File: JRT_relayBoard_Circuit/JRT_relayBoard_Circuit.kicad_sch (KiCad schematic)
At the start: 0 parts

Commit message: 回路図を実装
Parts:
- added J1: Conn_ESP32_Left, symbol Connector:Conn_01x15_Socket
- added J2: Conn_ESP32_Right, symbol Connector:Conn_01x15_Socket
- added J3: 37212-62M3-003PL, CONN_37212-62M3-003PL_3MM, symbol 37212_62M3_003PL:37212-62M3-003PL
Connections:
- new net +3.3V: J1.1 (Pin_1)
- new net +9V: J2.1 (Pin_1)
- new net A1: J2.10 (Pin_10)
- new net A2: J2.11 (Pin_11)
- new net A3: J2.12 (Pin_12)
- new net A4: J2.13 (Pin_13)
- new net A5: J2.14 (Pin_14)
- new net D1: J1.3 (Pin_3)
- new net D10: J2.4 (Pin_4)
- new net D11: J2.5 (Pin_5)
- new net D12: J2.6 (Pin_6)
- new net D13: J2.7 (Pin_7)
- new net D14: J2.8 (Pin_8)
- new net D15: J2.9 (Pin_9)
- new net D2: J1.5 (Pin_5)
- new net D3: J1.8 (Pin_8), J1.9 (Pin_9)
- new net D5: J1.10 (Pin_10)
- new net D6: J1.11 (Pin_11)
- new net D7: J1.14 (Pin_14)
- new net D8: J1.15 (Pin_15)
- new net D9: J2.3 (Pin_3)
- new net GND: J2.2 (Pin_2)
- new net GND1: J1.2 (Pin_2)
- new net UART-RX: J1.6 (Pin_6)
- new net UART-TX: J1.7 (Pin_7)
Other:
- note added: "ESP32関係の配線 (ELEGOO ESP-32 開発ボード)"
- company: (none) -> (一社)次世代ロボットエンジニア支援機構
- title: (none) -> JRT中継基板Ver2.0

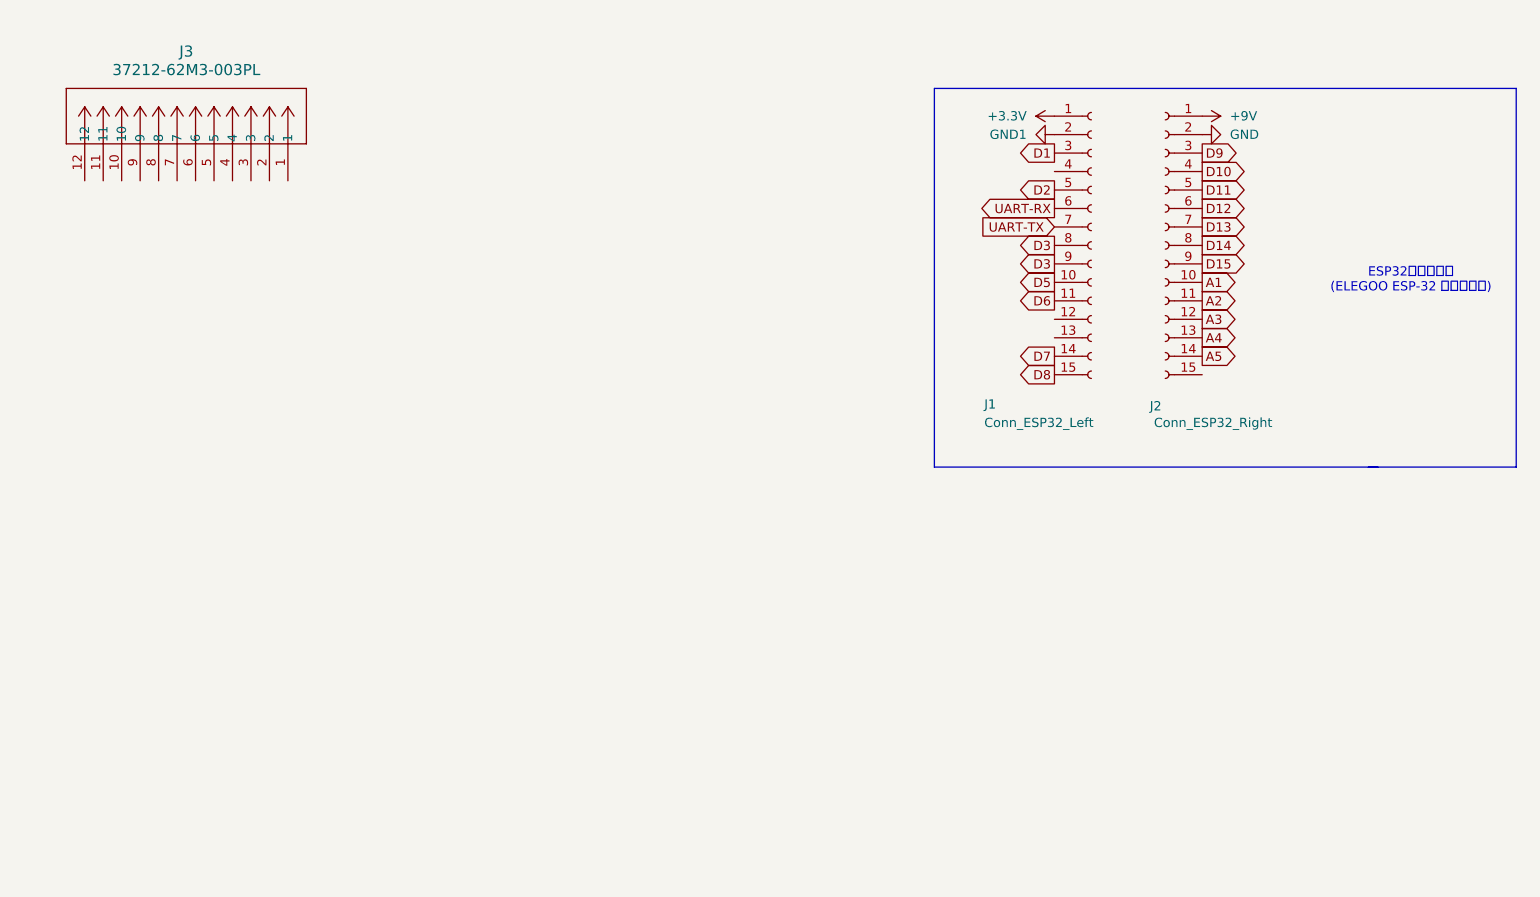
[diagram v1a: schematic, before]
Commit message: コネクタの配置をした
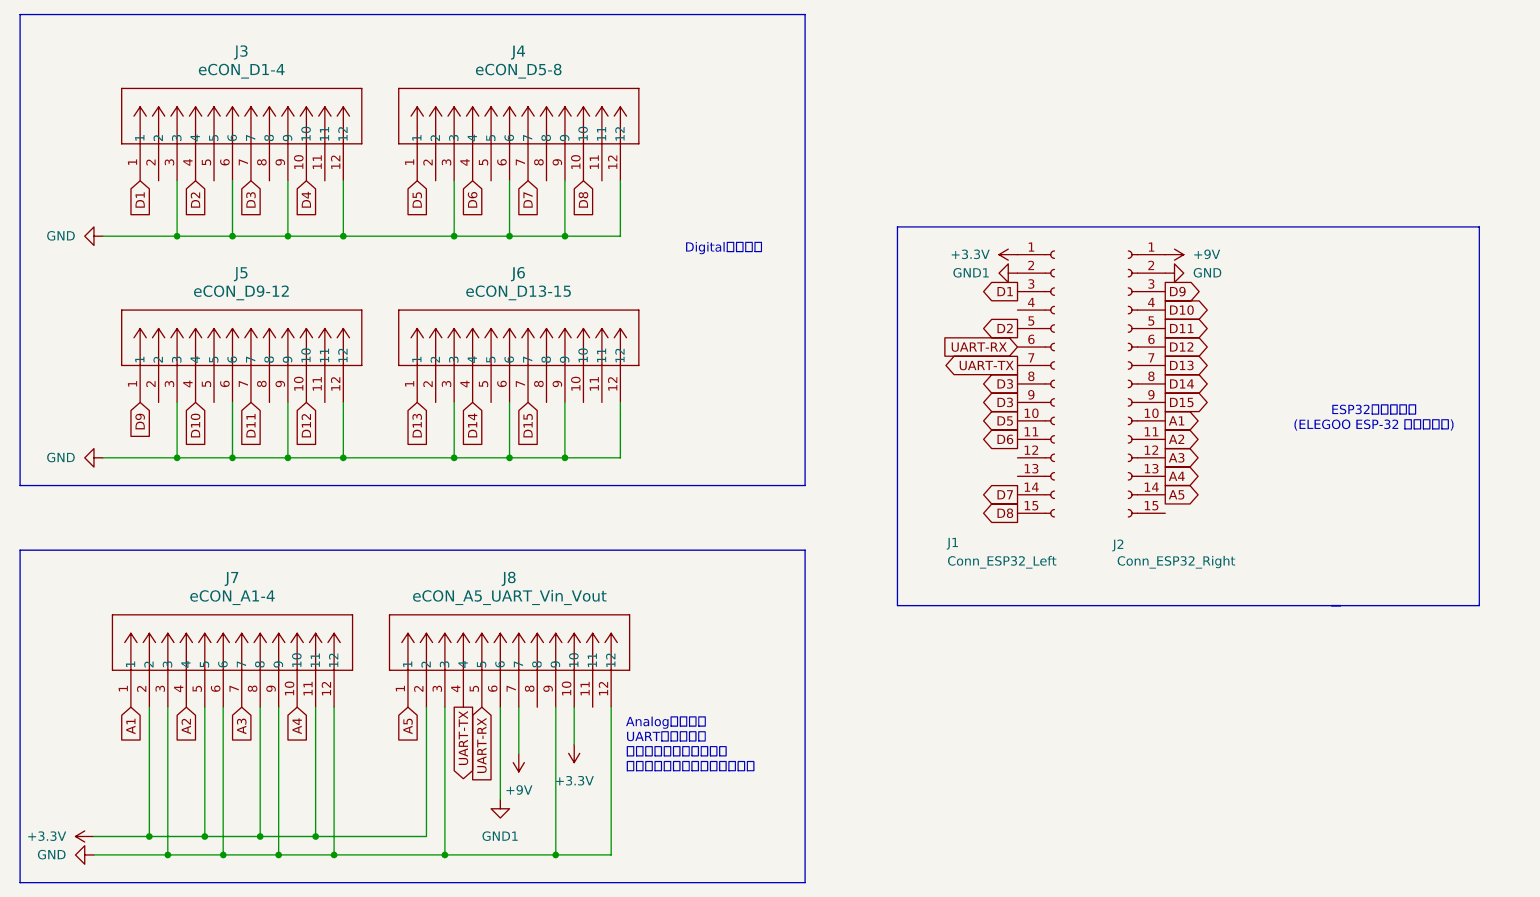
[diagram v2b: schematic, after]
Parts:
- added J4: eCON_D5-8, eCon:CONN_37212-62M3-003PL_3MM, symbol 37212_62M3_003PL:37212-62M3-003PL
- added J5: eCON_D9-12, eCon:CONN_37212-62M3-003PL_3MM, symbol 37212_62M3_003PL:37212-62M3-003PL
- added J6: eCON_D13-15, eCon:CONN_37212-62M3-003PL_3MM, symbol 37212_62M3_003PL:37212-62M3-003PL
- added J7: eCON_A1-4, eCon:CONN_37212-62M3-003PL_3MM, symbol 37212_62M3_003PL:37212-62M3-003PL
- added J8: eCON_A5_UART_Vin_Vout, eCon:CONN_37212-62M3-003PL_3MM, symbol 37212_62M3_003PL:37212-62M3-003PL
- J1, J2: footprint (none) -> Connector_PinSocket_2.54mm:PinSocket_1x15_P2.54mm_Vertical
- J3: value 37212-62M3-003PL -> eCON_D1-4; footprint CONN_37212-62M3-003PL_3MM -> eCon:CONN_37212-62M3-003PL_3MM
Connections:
- net +3.3V: now also J7.11, J7.2, J7.5, J7.8, J8.10, J8.2
- net +9V: now also J8.7
- net A1: now also J7.1
- net A2: now also J7.4
- net A3: now also J7.7
- net A4: now also J7.10
- net A5: now also J8.1
- net D1: now also J3.1
- net D10: now also J5.4
- net D11: now also J5.7
- net D12: now also J5.10
- net D13: now also J6.1
- net D14: now also J6.4
- net D15: now also J6.7
- net D2: now also J3.4
- net D3: now also J3.7
- net D5: now also J4.1
- net D6: now also J4.4
- net D7: now also J4.7
- net D8: now also J4.10
- net D9: now also J5.1
- net GND: now also J3.12, J3.3, J3.6, J3.9, J4.12, J4.3, J4.6, J4.9, J5.12, J5.3, J5.6, J5.9, J6.12, J6.3, J6.6, J6.9, J7.12, J7.3, J7.6, J7.9, J8.12, J8.3, J8.9
- net GND1: now also J8.6
- net UART-RX: now also J8.5
- net UART-TX: now also J8.4
- net D4: now reaches J3.10
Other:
- note added: "Analog入力端子 UART入出力端子 マイコン用電源入力端子 送信モジュール用電源出力端子"
- note added: "Digital入力端子"
- moved on the sheet: J1, J2, J3

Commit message: 配線を行った
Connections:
- net UART-RX: now also J8.4; no longer J8.5
- net UART-TX: now also J8.5; no longer J8.4

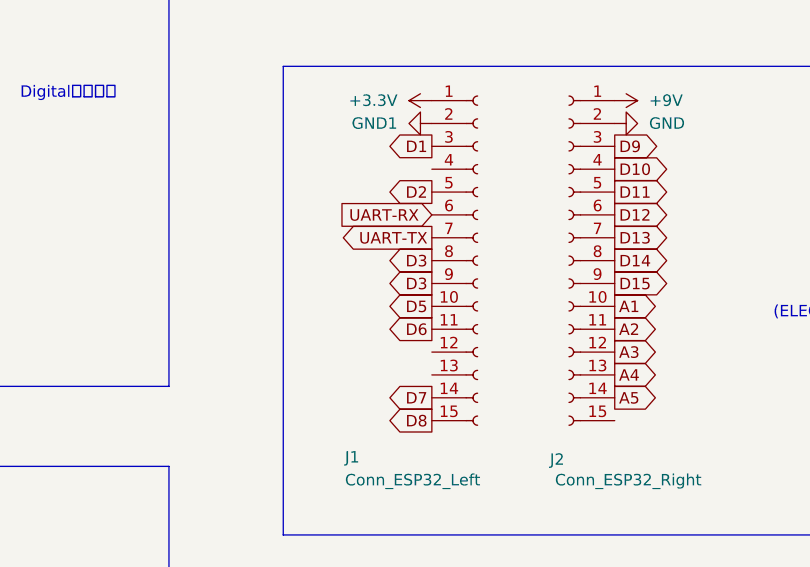
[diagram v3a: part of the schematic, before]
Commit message: 基板上のシルクを追加
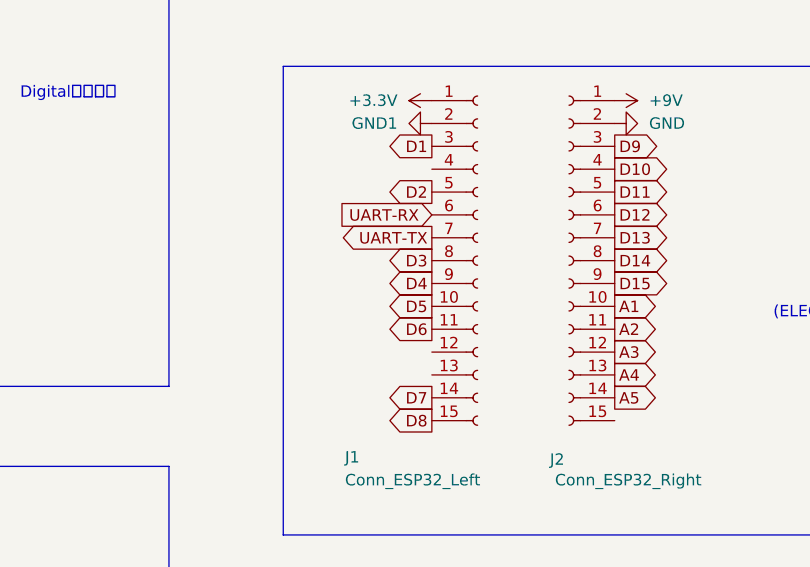
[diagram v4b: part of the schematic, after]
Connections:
- net D3: no longer J1.9 (Pin_9)
- net D4: now also J1.9 (Pin_9)
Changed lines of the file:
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@@
 		)
 	)
-	(global_label "D3"
+	(global_label "D4"
 		(shape output)
 		(at 190.5 85.09 180)

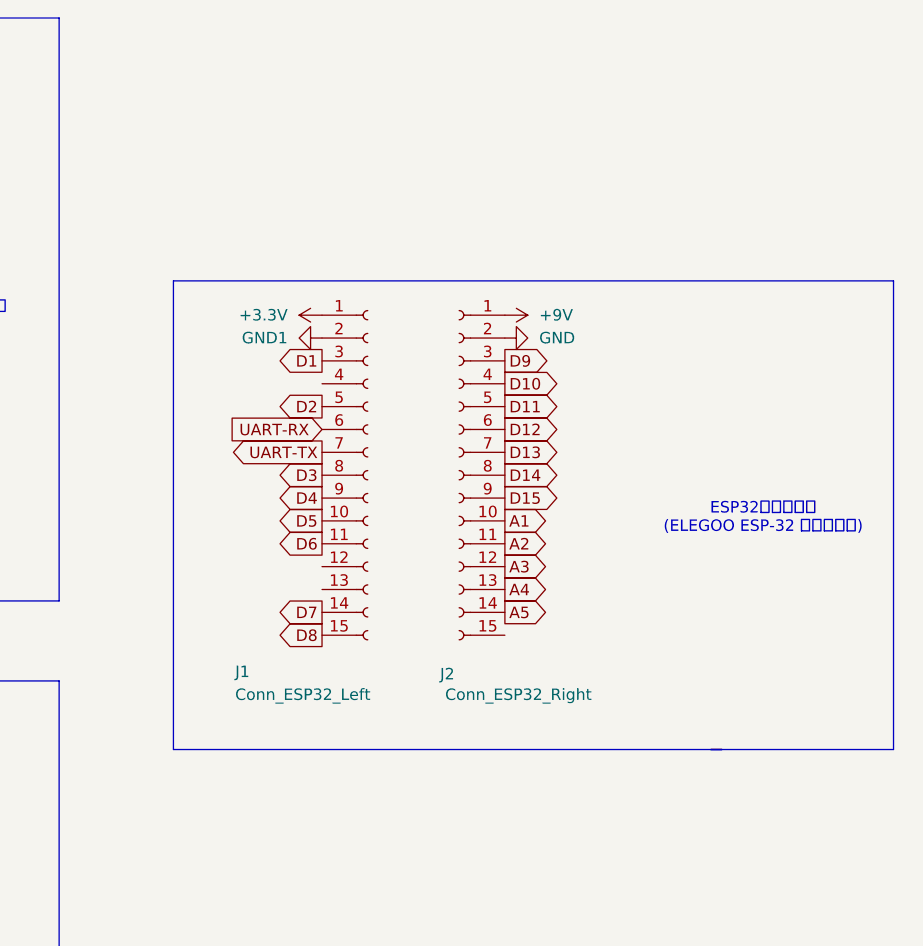
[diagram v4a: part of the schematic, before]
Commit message: 電源スイッチ取付用穴を追加
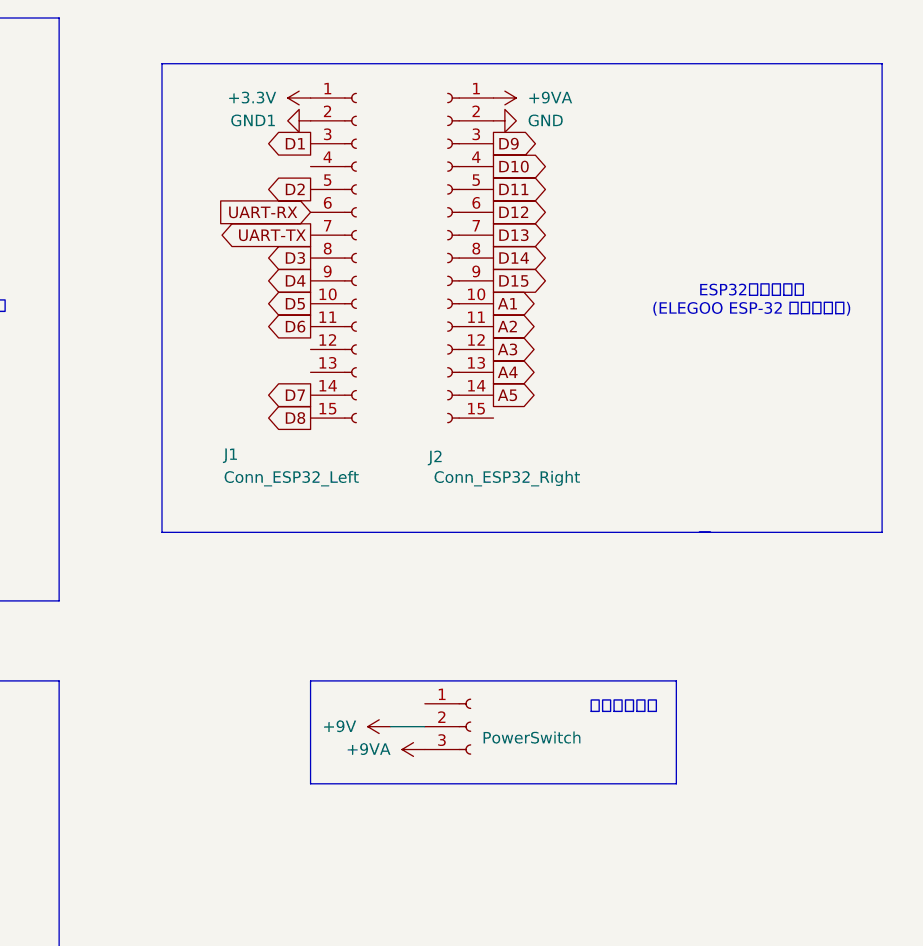
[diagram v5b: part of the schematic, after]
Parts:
- added J9: PowerSwitch, Connector_PinSocket_2.54mm:PinSocket_1x03_P2.54mm_Vertical, symbol Connector:Conn_01x03_Socket
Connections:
- net +9V: now also J9.2 (Pin_2); no longer J2.1 (Pin_1)
- new net +9VA: J2.1 (Pin_1), J9.3 (Pin_3)
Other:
- note added: "電源スイッチ"
- moved on the sheet: J1, J2
